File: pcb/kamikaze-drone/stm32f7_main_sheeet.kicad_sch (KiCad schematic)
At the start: 17 parts, among them J1 SWD Connector, SW1 SW_NRST, SW2 SW_BOOT0, U1 STM32F765VITx, Y1 25 MHz

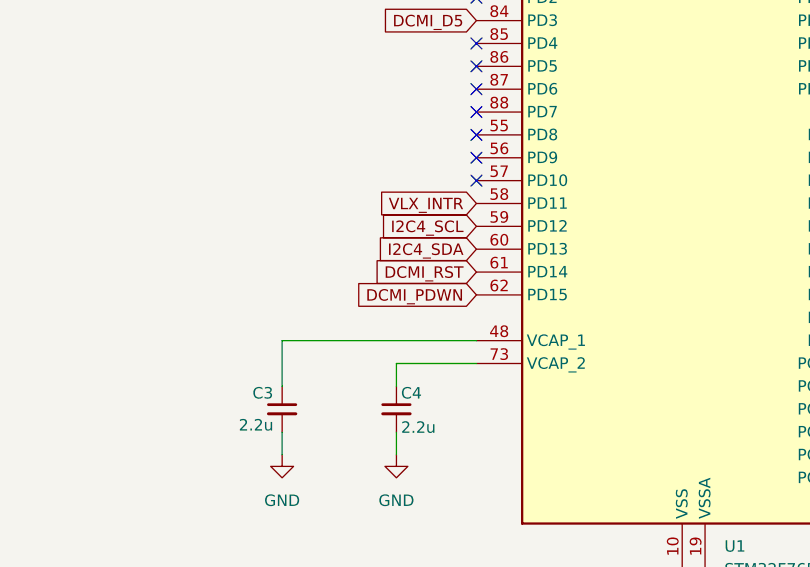
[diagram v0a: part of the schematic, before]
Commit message: WIP - arranging components in updated PCB
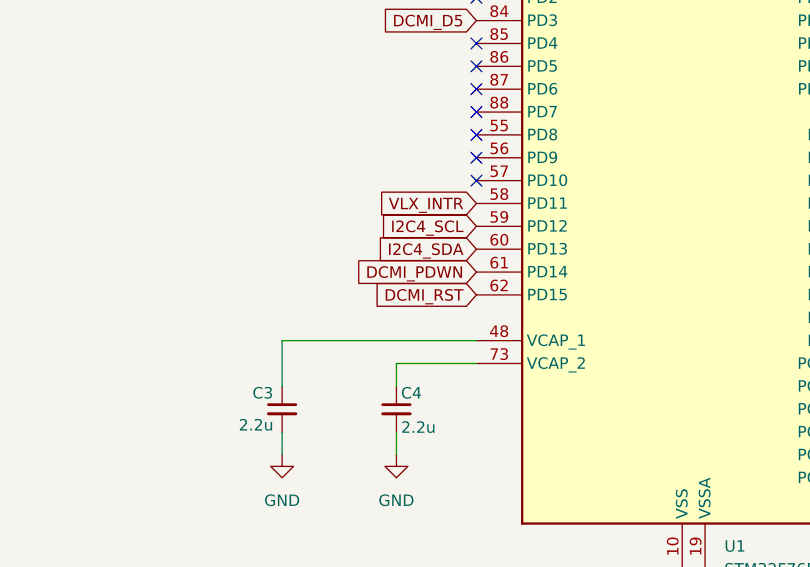
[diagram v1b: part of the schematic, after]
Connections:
- net DCMI_PDWN: now also U1.61 (PD14); no longer U1.62 (PD15)
- net DCMI_RST: now also U1.62 (PD15); no longer U1.61 (PD14)
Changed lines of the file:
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@@
 	(global_label "DCMI_RST"
 		(shape input)
+		(at 74.93 148.59 180)
+		(fields_autoplaced yes)
+		(effects
+			(font
+				(size 1.27 1.27)
+			)
+			(justify right)
+		)
+		(property "Intersheetrefs" "${INTERSHEET_REFS}"
+			(at 62.9339 148.59 0)
+			(effects
+				(font
+					(size 1.27 1.27)
+				)
+				(justify right)
+				(hide yes)
+			)
+		)
+	)
+	(global_label "M2_SIG"
+		(shape input)
+		(at 120.65 69.85 0)
+		(fields_autoplaced yes)
+		(effects
+			(font
+				(size 1.27 1.27)
+			)
+			(justify left)
+		)
+		(property "Intersheetrefs" "${INTERSHEET_REFS}"
+			(at 130.348 69.85 0)
+			(effects
+				(font
+					(size 1.27 1.27)
+				)
+				(justify left)
+				(hide yes)
+			)
+		)
+	)
+	(global_label "PAYLOAD"
+		(shape input)
+		(at 120.65 118.11 0)
+		(fields_autoplaced yes)
+		(effects
+			(font
+				(size 1.27 1.27)
+			)
+			(justify left)
+		)
+		(property "Intersheetrefs" "${INTERSHEET_REFS}"
+			(at 131.7996 118.11 0)
+			(effects
+				(font
+					(size 1.27 1.27)
+				)
+				(justify left)
+				(hide yes)
+			)
+		)
+	)
+	(global_label "BOOT0"
+		(shape input)
+		(at 241.3 50.8 180)
+		(fields_autoplaced yes)
+		(effects
+			(font
+				(size 1.27 1.27)
+			)
+			(justify right)
+		)
+		(property "Intersheetrefs" "${INTERSHEET_REFS}"
+			(at 232.2067 50.8 0)
+			(effects
+				(font
+					(size 1.27 1.27)
+				)
+				(justify right)
+				(hide yes)
+			)
+		)
+	)
+	(global_label "PAYLOAD"
+		(shape input)
+		(at 226.06 120.65 270)
+		(fields_autoplaced yes)
+		(effects
+			(font
+				(size 1.27 1.27)
+			)
+			(justify right)
+		)
+		(property "Intersheetrefs" "${INTERSHEET_REFS}"
+			(at 226.06 131.7996 90)
+			(effects
+				(font
+					(size 1.27 1.27)
+				)
+				(justify right)
+				(hide yes)
+			)
+		)
+	)
+	(global_label "DCMI_D1"
+		(shape input)
+		(at 120.65 148.59 0)
+		(fields_autoplaced yes)
+		(effects
+			(font
+				(size 1.27 1.27)
+			)
+			(justify left)
+		)
+		(property "Intersheetrefs" "${INTERSHEET_REFS}"
+			(at 131.6785 148.59 0)
+			(effects
+				(font
+					(size 1.27 1.27)
+				)
+				(justify left)
+				(hide yes)
+			)
+		)
+	)
+	(global_label "VLX_INTR"
+		(shape input)
+		(at 74.93 138.43 180)
+		(fields_autoplaced yes)
+		(effects
+			(font
+				(size 1.27 1.27)
+			)
+			(justify right)
+		)
+		(property "Intersheetrefs" "${INTERSHEET_REFS}"
+			(at 63.4781 138.43 0)
+			(effects
+				(font
+					(size 1.27 1.27)
+				)
+				(justify right)
+				(hide yes)
+			)
+		)
+	)
+	(global_label "SWD_NRST"
+		(shape input)
+		(at 74.93 44.45 180)
+		(fields_autoplaced yes)
+		(effects
+			(font
+				(size 1.27 1.27)
+			)
+			(justify right)
+		)
+		(property "Intersheetrefs" "${INTERSHEET_REFS}"
+			(at 62.2687 44.45 0)
+			(effects
+				(font
+					(size 1.27 1.27)
+				)
+				(justify right)
+				(hide yes)
+			)
+		)
+	)
+	(global_label "DCMI_HSYNC"
+		(shape input)
+		(at 120.65 54.61 0)
+		(fields_autoplaced yes)
+		(effects
+			(font
+				(size 1.27 1.27)
+			)
+			(justify left)
+		)
+		(property "Intersheetrefs" "${INTERSHEET_REFS}"
+			(at 135.4281 54.61 0)
+			(effects
+				(font
+					(size 1.27 1.27)
+				)
+				(justify left)
+				(hide yes)
+			)
+		)
+	)
+	(global_label "DCMI_PDWN"
+		(shape input)
 		(at 74.93 146.05 180)
 		(fields_autoplaced yes)
@@
 		)
 		(property "Intersheetrefs" "${INTERSHEET_REFS}"
-			(at 62.9339 146.05 0)
-			(effects
-				(font
-					(size 1.27 1.27)
-				)
-				(justify right)
-				(hide yes)
-			)
-		)
-	)
-	(global_label "M2_SIG"
-		(shape input)
-		(at 120.65 69.85 0)
-		(fields_autoplaced yes)
-		(effects
-			(font
-				(size 1.27 1.27)
-			)
-			(justify left)
-		)
-		(property "Intersheetrefs" "${INTERSHEET_REFS}"
-			(at 130.348 69.85 0)
-			(effects
-				(font
-					(size 1.27 1.27)
-				)
-				(justify left)
-				(hide yes)
-			)
-		)
-	)
-	(global_label "PAYLOAD"
-		(shape input)
-		(at 120.65 118.11 0)
-		(fields_autoplaced yes)
-		(effects
-			(font
-				(size 1.27 1.27)
-			)
-			(justify left)
-		)
-		(property "Intersheetrefs" "${INTERSHEET_REFS}"
-			(at 131.7996 118.11 0)
-			(effects
-				(font
-					(size 1.27 1.27)
-				)
-				(justify left)
-				(hide yes)
-			)
-		)
-	)
-	(global_label "BOOT0"
-		(shape input)
-		(at 241.3 50.8 180)
-		(fields_autoplaced yes)
-		(effects
-			(font
-				(size 1.27 1.27)
-			)
-			(justify right)
-		)
-		(property "Intersheetrefs" "${INTERSHEET_REFS}"
-			(at 232.2067 50.8 0)
-			(effects
-				(font
-					(size 1.27 1.27)
-				)
-				(justify right)
-				(hide yes)
-			)
-		)
-	)
-	(global_label "PAYLOAD"
-		(shape input)
-		(at 226.06 120.65 270)
-		(fields_autoplaced yes)
-		(effects
-			(font
-				(size 1.27 1.27)
-			)
-			(justify right)
-		)
-		(property "Intersheetrefs" "${INTERSHEET_REFS}"
-			(at 226.06 131.7996 90)
-			(effects
-				(font
-					(size 1.27 1.27)
-				)
-				(justify right)
-				(hide yes)
-			)
-		)
-	)
-	(global_label "DCMI_D1"
-		(shape input)
-		(at 120.65 148.59 0)
-		(fields_autoplaced yes)
-		(effects
-			(font
-				(size 1.27 1.27)
-			)
-			(justify left)
-		)
-		(property "Intersheetrefs" "${INTERSHEET_REFS}"
-			(at 131.6785 148.59 0)
-			(effects
-				(font
-					(size 1.27 1.27)
-				)
-				(justify left)
-				(hide yes)
-			)
-		)
-	)
-	(global_label "VLX_INTR"
-		(shape input)
-		(at 74.93 138.43 180)
-		(fields_autoplaced yes)
-		(effects
-			(font
-				(size 1.27 1.27)
-			)
-			(justify right)
-		)
-		(property "Intersheetrefs" "${INTERSHEET_REFS}"
-			(at 63.4781 138.43 0)
-			(effects
-				(font
-					(size 1.27 1.27)
-				)
-				(justify right)
-				(hide yes)
-			)
-		)
-	)
-	(global_label "SWD_NRST"
-		(shape input)
-		(at 74.93 44.45 180)
-		(fields_autoplaced yes)
-		(effects
-			(font
-				(size 1.27 1.27)
-			)
-			(justify right)
-		)
-		(property "Intersheetrefs" "${INTERSHEET_REFS}"
-			(at 62.2687 44.45 0)
-			(effects
-				(font
-					(size 1.27 1.27)
-				)
-				(justify right)
-				(hide yes)
-			)
-		)
-	)
-	(global_label "DCMI_HSYNC"
-		(shape input)
-		(at 120.65 54.61 0)
-		(fields_autoplaced yes)
-		(effects
-			(font
-				(size 1.27 1.27)
-			)
-			(justify left)
-		)
-		(property "Intersheetrefs" "${INTERSHEET_REFS}"
-			(at 135.4281 54.61 0)
-			(effects
-				(font
-					(size 1.27 1.27)
-				)
-				(justify left)
-				(hide yes)
-			)
-		)
-	)
-	(global_label "DCMI_PDWN"
-		(shape input)
-		(at 74.93 148.59 180)
-		(fields_autoplaced yes)
-		(effects
-			(font
-				(size 1.27 1.27)
-			)
-			(justify right)
-		)
-		(property "Intersheetrefs" "${INTERSHEET_REFS}"
-			(at 61.0591 148.59 0)
-			(effects
-				(font
+			(at 61.0591 146.05 0)
+			(effects
+				(font

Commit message: WIP - Power routing done. Signal routing remaining
- Power routing from USB and battery to MCP and AMS completed.
- Power routing from motors to battery completed
- Grounds have not been routed yet, leaving to the end.
- Most 3V3 pads haven't been routed yet, leaving to the end
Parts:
- SW1: footprint Button_Switch_SMD:SW_DIP_SPSTx01_Slide_6.7x4.1mm_W6.73mm_P2.54mm_LowProfile_JPin -> kamikaze_drone_custom_footprints:button-footprint
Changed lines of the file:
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@@
 			)
 		)
-		(property "Footprint" "Button_Switch_SMD:SW_DIP_SPSTx01_Slide_6.7x4.1mm_W6.73mm_P2.54mm_LowProfile_JPin"
+		(property "Footprint" "kamikaze_drone_custom_footprints:button-footprint"
 			(at 255.27 30.48 0)
 			(effects

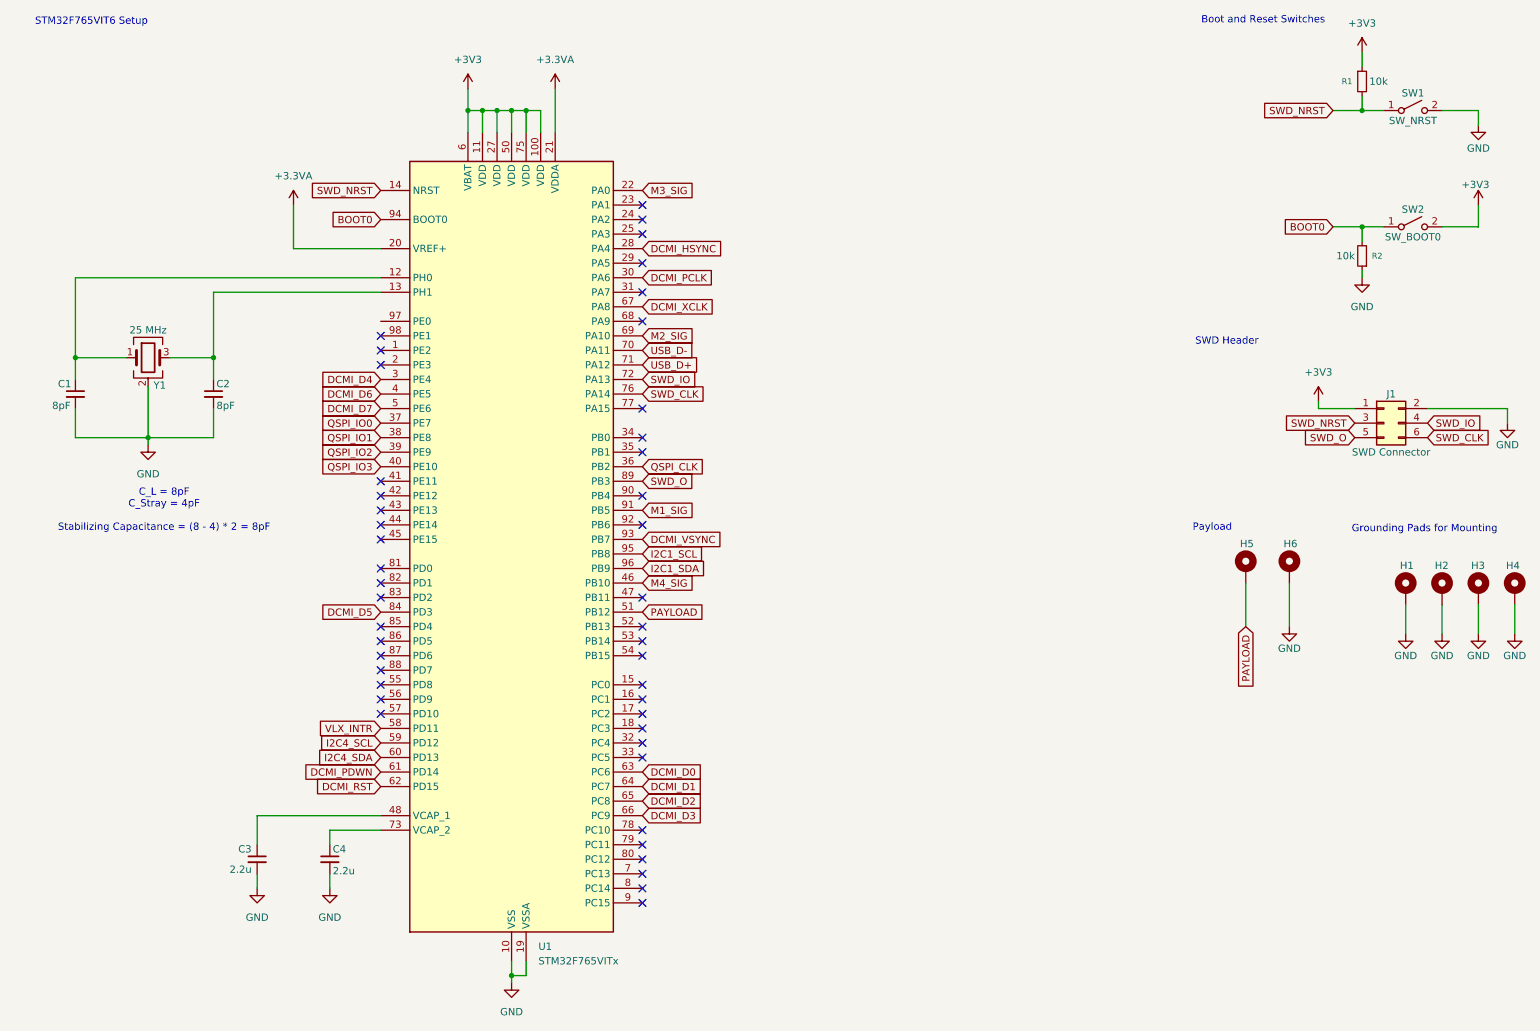
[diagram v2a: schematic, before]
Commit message: v2.0 of PCB completed
Updated routing to have USB port in center of top.
Shrank overall size to 50x50 mm
Layout is now ground+signal >> ground >> 3V3 >> signal

TODO: Add stitching vias between ground on top and second layer?
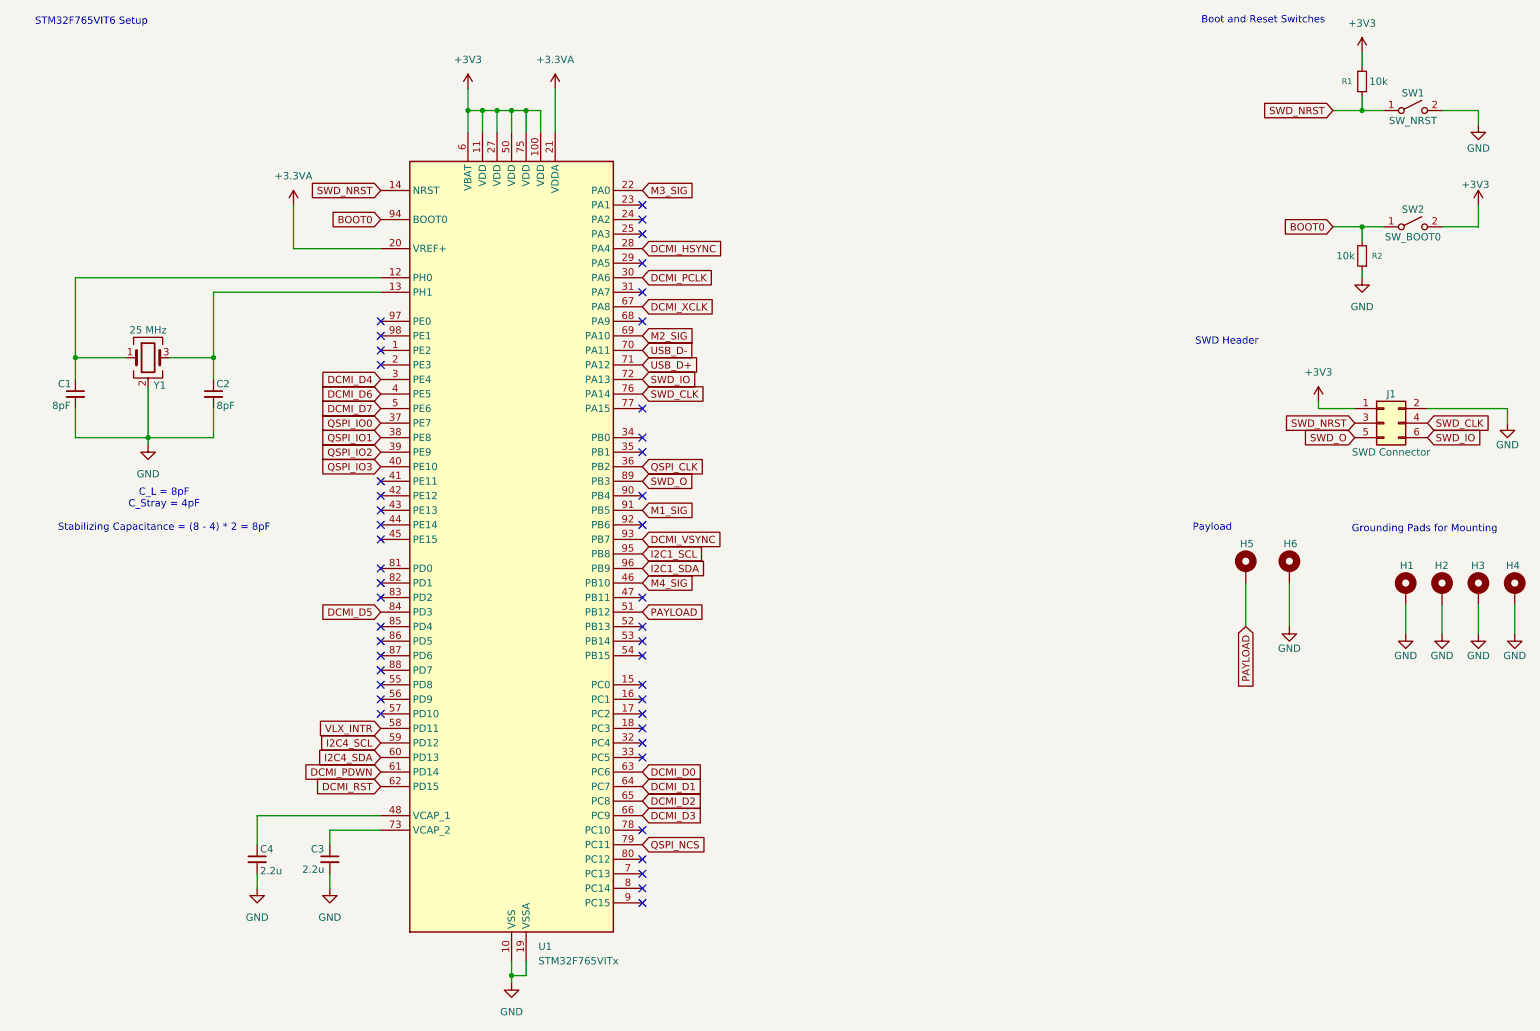
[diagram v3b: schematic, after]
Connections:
- net SWD_CLK: now also J1.4 (Pin_4); no longer J1.6 (Pin_6)
- net SWD_IO: now also J1.6 (Pin_6); no longer J1.4 (Pin_4)
- net at U1.48 (VCAP_1): now also C4.1; no longer C3.1
- net at U1.73 (VCAP_2): now also C3.1; no longer C4.1
- net QSPI_NCS: now reaches U1.79 (PC11)
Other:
- moved on the sheet: C3, C4
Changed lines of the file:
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@@
 	(title_block
 		(title "STM32F765VIT6 General Configuration")
-		(date "2026-05-21")
-		(rev "v1.0")
+		(date "2026-05-24")
+		(rev "v2.0")
 		(company "Pranav Chandra N. V.")
 		(comment 1 "v1.0 - First Iteration")
+		(comment 2 "v2.0 - Connected QSPI properly and updated nrst switch footprint")
 	)
 	(text "Payload\n"
@@
 			(font
 				(size 1.27 1.27)
-				(color 255 13 4 1)
+				(color 255 0 255 1)
 			)
 		)
@@
 	)
 	(no_connect
+		(at 74.93 67.31)
+	)
+	(no_connect
 		(at 120.65 130.81)
 	)
@@
 	)
 	(no_connect
-		(at 120.65 158.75)
-	)
-	(no_connect
 		(at 74.93 72.39)
 	)
@@
 	(global_label "SWD_CLK"
 		(shape input)
-		(at 257.81 87.63 0)
+		(at 257.81 85.09 0)
 		(fields_autoplaced yes)
 		(effects
@@
 		)
 		(property "Intersheetrefs" "${INTERSHEET_REFS}"
-			(at 269.2618 87.63 0)
+			(at 269.2618 85.09 0)
 			(effects
 				(font
@@
 		)
 	)
+	(global_label "QSPI_NCS"
+		(shape input)
+		(at 120.65 158.75 0)
+		(fields_autoplaced yes)
+		(effects
+			(font
+				(size 1.27 1.27)
+			)
+			(justify left)
+		)
+		(property "Intersheetrefs" "${INTERSHEET_REFS}"
+			(at 132.8276 158.75 0)
+			(effects
+				(font
+					(size 1.27 1.27)
+				)
+				(justify left)
+				(hide yes)
+			)
+		)
+	)
 	(global_label "DCMI_HSYNC"
 		(shape input)
@@
 	(global_label "SWD_IO"
 		(shape input)
-		(at 257.81 85.09 0)
+		(at 257.81 87.63 0)
 		(fields_autoplaced yes)
 		(effects
@@
 		)
 		(property "Intersheetrefs" "${INTERSHEET_REFS}"
-			(at 267.629 85.09 0)
+			(at 267.629 87.63 0)
 			(effects
 				(font
@@
 	(symbol
 		(lib_id "Device:C_Small")
-		(at 53.34 161.29 0)
+		(at 66.04 161.29 0)
 		(unit 1)
 		(exclude_from_sim no)
@@
 		(dnp no)
 		(property "Reference" "C3"
-			(at 50.038 159.512 0)
+			(at 62.738 159.512 0)
 			(effects
 				(font
@@
 		)
 		(property "Value" "2.2u"
-			(at 48.514 163.068 0)
+			(at 61.214 163.068 0)
 			(effects
 				(font
@@
 		)
 		(property "Footprint" "Capacitor_SMD:C_0805_2012Metric_Pad1.18x1.45mm_HandSolder"
-			(at 53.34 161.29 0)
+			(at 66.04 161.29 0)
 			(effects
 				(font
@@
 		)
 		(property "Datasheet" "~"
-			(at 53.34 161.29 0)
+			(at 66.04 161.29 0)
 			(effects
 				(font
@@
 		)
 		(property "Description" "Unpolarized capacitor, small symbol"
-			(at 53.34 161.29 0)
+			(at 66.04 161.29 0)
 			(effects
 				(font
@@
 		)
 		(property "Robu SKU" "R153134"
-			(at 53.34 161.29 0)
+			(at 66.04 161.29 0)
 			(effects
 				(font
@@
 	(symbol
 		(lib_id "Device:C_Small")
-		(at 66.04 161.29 0)
+		(at 53.34 161.29 0)
 		(unit 1)
 		(exclude_from_sim no)
@@
 		(dnp no)
 		(property "Reference" "C4"
-			(at 66.548 159.512 0)
+			(at 53.848 159.512 0)
 			(effects
 				(font
@@
 		)
 		(property "Value" "2.2u"
-			(at 66.548 163.322 0)
+			(at 53.848 163.322 0)
 			(effects
 				(font
@@
 		)
 		(property "Footprint" "Capacitor_SMD:C_0805_2012Metric_Pad1.18x1.45mm_HandSolder"
-			(at 66.04 161.29 0)
+			(at 53.34 161.29 0)
 			(effects
 				(font
@@
 		)
 		(property "Datasheet" "~"
-			(at 66.04 161.29 0)
+			(at 53.34 161.29 0)
 			(effects
 				(font
@@
 		)
 		(property "Description" "Unpolarized capacitor, small symbol"
-			(at 66.04 161.29 0)
+			(at 53.34 161.29 0)
 			(effects
 				(font
@@
 		)
 		(property "Robu SKU" "R153134"
-			(at 66.04 161.29 0)
+			(at 53.34 161.29 0)
 			(effects
 				(font
